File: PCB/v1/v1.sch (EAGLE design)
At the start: 45 parts, among them U2 AT24C512C-SHD-B

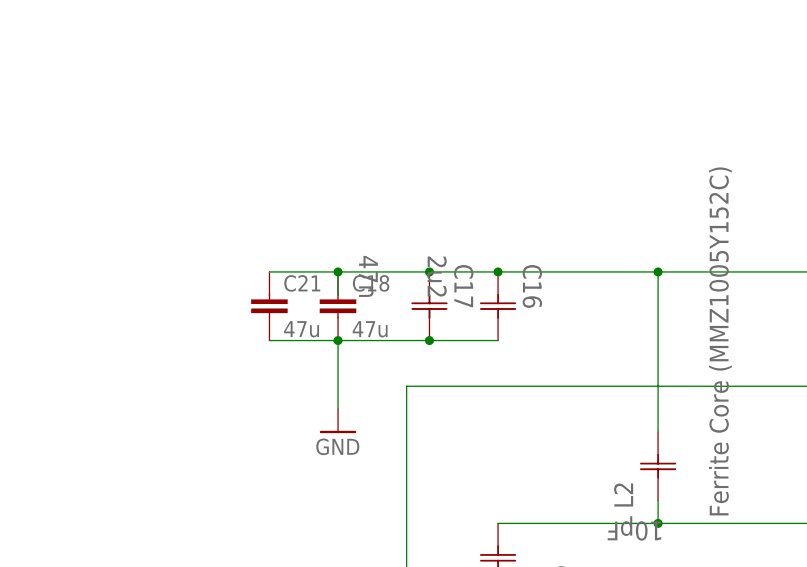
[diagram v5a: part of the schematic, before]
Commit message: board submitted (albeit without tstop over QFN pad
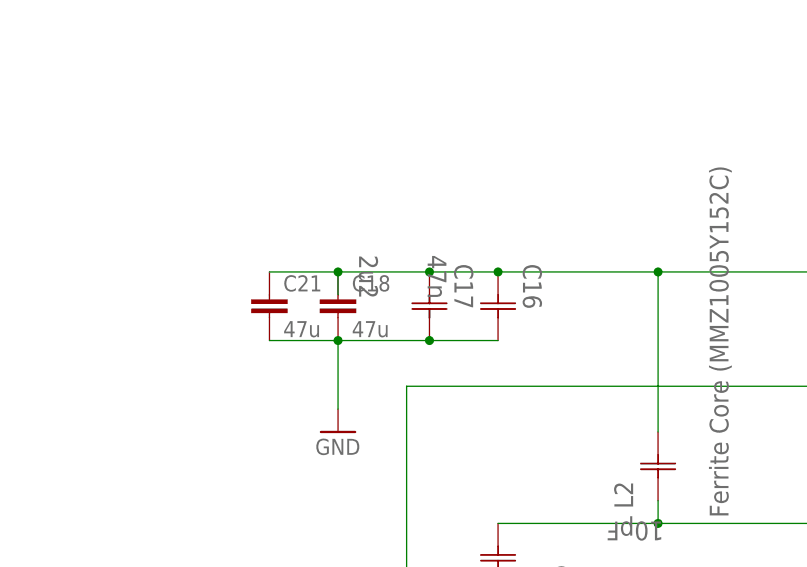
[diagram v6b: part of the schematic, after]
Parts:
- C16: value 2u2 -> 47n
- C17: value 47n -> 2u2
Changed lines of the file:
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@@
 <part name="C14" library="AVX_By_element14_Batch_1" deviceset="UQCL2A100JAT2A/500" device="" value="470n"/>
 <part name="GND9" library="supply1" deviceset="GND" device=""/>
-<part name="C16" library="AVX_By_element14_Batch_1" deviceset="UQCL2A1R0BAT2A/500" device="" value="2u2"/>
+<part name="C16" library="AVX_By_element14_Batch_1" deviceset="UQCL2A1R0BAT2A/500" device="" value="47n"/>
 <part name="GND10" library="supply1" deviceset="GND" device=""/>
 <part name="VDD2" library="supply1" deviceset="VDD" device=""/>
@@
 <part name="C21" library="resistor" deviceset="C-EU" device="C0805" value="47u"/>
 <part name="C22" library="AVX_By_element14_Batch_1" deviceset="UQCL2A0R5BAT2A/500" device="" value="2.7 pF"/>
-<part name="C17" library="AVX_By_element14_Batch_1" deviceset="UQCL2A1R0BAT2A/500" device="" value="47n"/>
+<part name="C17" library="AVX_By_element14_Batch_1" deviceset="UQCL2A1R0BAT2A/500" device="" value="2u2"/>
 <part name="GND8" library="supply1" deviceset="GND" device=""/>
 <part name="GND11" library="supply1" deviceset="GND" device=""/>

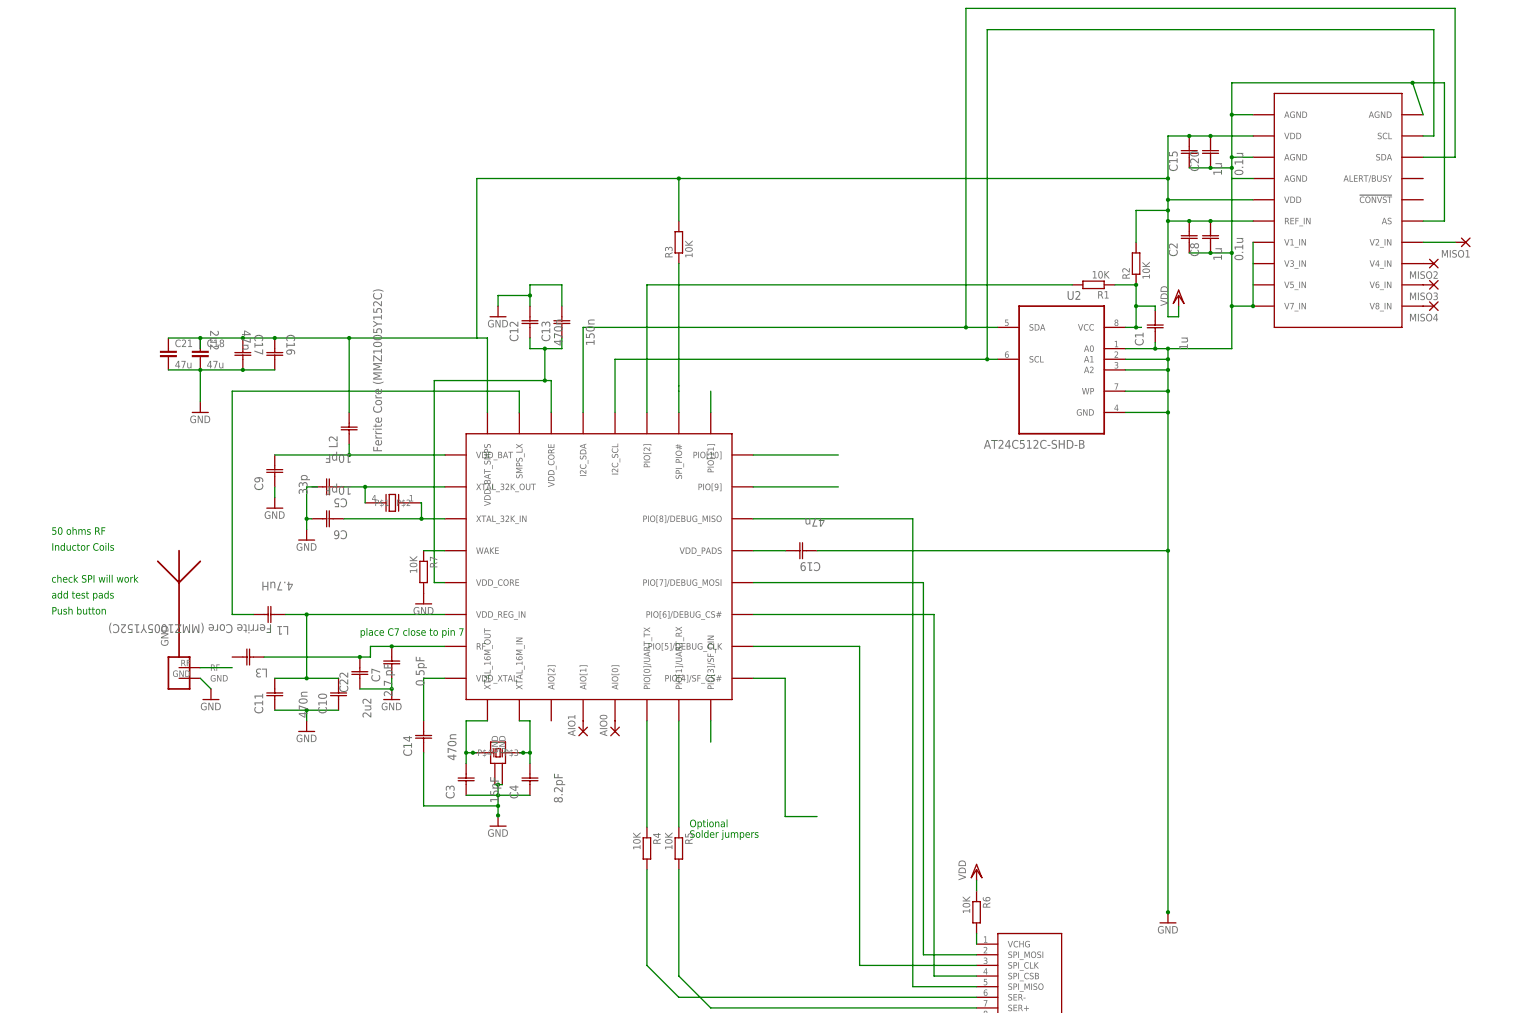
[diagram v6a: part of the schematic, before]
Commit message: added ADC and battery holder to schem
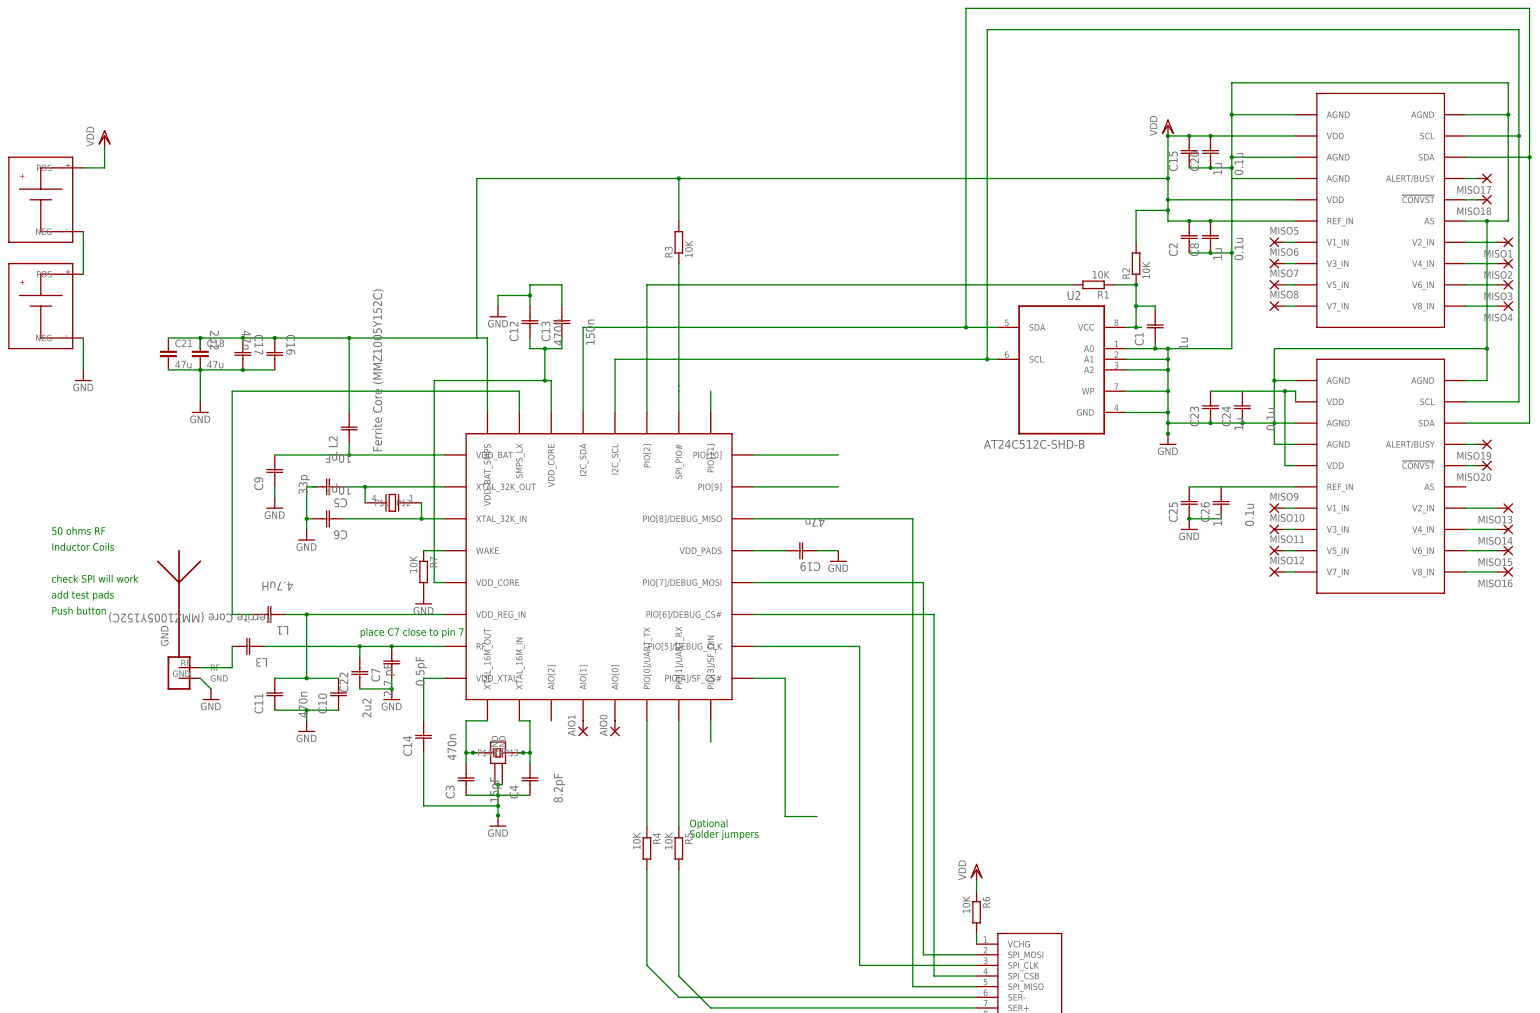
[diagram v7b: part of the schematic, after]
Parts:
- added C23, C25: 1u, AVX_By_element14_Batch_1:UQCL2A100JAT2A/500
- added C24, C26: 0.1u, AVX_By_element14_Batch_1:UQCL2A100JAT2A/500
- added MISO10, MISO11, MISO12, MISO13, MISO14, MISO15, MISO16, MISO17, MISO18, MISO19, MISO20, MISO5, MISO6, MISO7, MISO8, MISO9: (no value), wirepad:1,6/0,8
- added U$6: AD7997, AD7997:AD7997
- added U$7, U$8: BATTERY_2996, BATTERY_2996:BATTERY_2996
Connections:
- new net N$10: C25.C2, U$6.REF_IN
- new net N$138: U$7.NEG, U$8.POS
- new net N$139: MISO5.P, U$5.V1_IN
- new net N$140: MISO6.P, U$5.V3_IN
- new net N$141: MISO7.P, U$5.V5_IN
- new net N$142: MISO8.P, U$5.V7_IN
- new net N$143: MISO9.P
- new net N$144: MISO10.P
- new net N$145: MISO11.P
- new net N$146: MISO12.P
- new net N$147: MISO13.P
- new net N$148: MISO15.P
- new net N$149: MISO14.P
- new net N$150: MISO16.P
- new net N$151: MISO17.P, U$5.ALERT/BUSY
- new net N$152: MISO18.P, U$5.!CONVST
- new net N$153: MISO19.P
- new net N$154: MISO20.P
- new net N$34: L3.C2
- new net N$8: C23.C2, U$6.VDD@1, U$6.VDD@2
- net GND: now also C23.C1, C24.C1, C25.C1, C26.C1, U$6.AGND@1, U$6.AGND@2, U$6.AGND@3, U$6.AGND@4; no longer U$5.V1_IN, U$5.V7_IN
- net SCL: now also U$6.SCL
- net SDA: now also U$6.SDA
- net VDD: now also U$7.POS
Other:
- moved on the sheet: L3, MISO1, MISO2, MISO3, MISO4

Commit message: added new ADC along with contact points
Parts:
- removed AIO0, AIO1, MISO1, MISO10, MISO11, MISO12, MISO13, MISO14, MISO15, MISO16, MISO17, MISO18, MISO19, MISO2, MISO20, MISO3, MISO4, MISO5, MISO6, MISO7, MISO8, MISO9: (no value), wirepad:1,6/0,8
- added R10, R11, R12, R13: 10K, rcl:R-EU_R0402
- added U$10, U$11, U$12, U$13, U$14, U$15, U$16, U$17, U$18, U$19, U$20, U$21, U$22, U$23, U$24, U$25, U$26, U$27, U$28, U$29, U$30, U$9: TEST_POINT_0.5MM, TEST_POINT_0.5mm:TEST_POINT_0.5MM
- U$7, U$8: device BATTERY_2996:BATTERY_2996 -> BATTERY_2996_2:BATTERY_2996
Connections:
- removed net N$143: MISO9.P
- removed net N$144: MISO10.P
- removed net N$145: MISO11.P
- removed net N$146: MISO12.P
- removed net N$147: MISO13.P
- removed net N$148: MISO15.P
- removed net N$149: MISO14.P
- removed net N$150: MISO16.P
- removed net N$153: MISO19.P
- removed net N$154: MISO20.P
- new net N$106: U$12.P$1, U$6.V8_IN
- new net N$108: R10.2
- new net N$110: R11.2
- new net N$113: R13.2
- new net N$117: U$11.P$1, U$6.V6_IN
- new net N$118: U$10.P$1, U$6.V4_IN
- new net N$12: U$14.P$1, U$6.V3_IN
- new net N$137: U$6.V2_IN, U$9.P$1
- new net N$14: U$13.P$1, U$6.V1_IN
- new net N$16: U$15.P$1, U$6.V5_IN
- new net N$90: U$16.P$1, U$6.V7_IN
- net GND: now also U$7.NEG
- net N$138: now also U$7.POS, U$8.NEG; no longer U$7.NEG, U$8.POS
- net N$139: now also U$21.P$1; no longer MISO5.P
- net N$140: now also U$22.P$1; no longer MISO6.P
- net N$141: now also U$23.P$1; no longer MISO7.P
- net N$142: now also U$24.P$1; no longer MISO8.P
- net N$151: no longer MISO17.P
- net N$152: no longer MISO18.P
- net N$18: now also U$25.P$1
- net N$28: now also U$1.AIO[1], U$29.P$1; no longer AIO0.P, U$1.AIO[0]
- net N$31: now also U$27.P$1
- net N$33: now also U$1.AIO[0], U$30.P$1; no longer AIO1.P, U$1.AIO[1]
- net N$46: now also U$17.P$1; no longer MISO1.P
- net N$50: now also U$26.P$1
- net N$51: now also U$28.P$1
- net N$73: now also U$19.P$1; no longer MISO3.P
- net N$82: now also U$18.P$1; no longer MISO2.P
- net N$83: now also U$20.P$1; no longer MISO4.P
- net VDD: now also U$8.POS; no longer U$7.POS
